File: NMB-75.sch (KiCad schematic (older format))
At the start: 20 parts

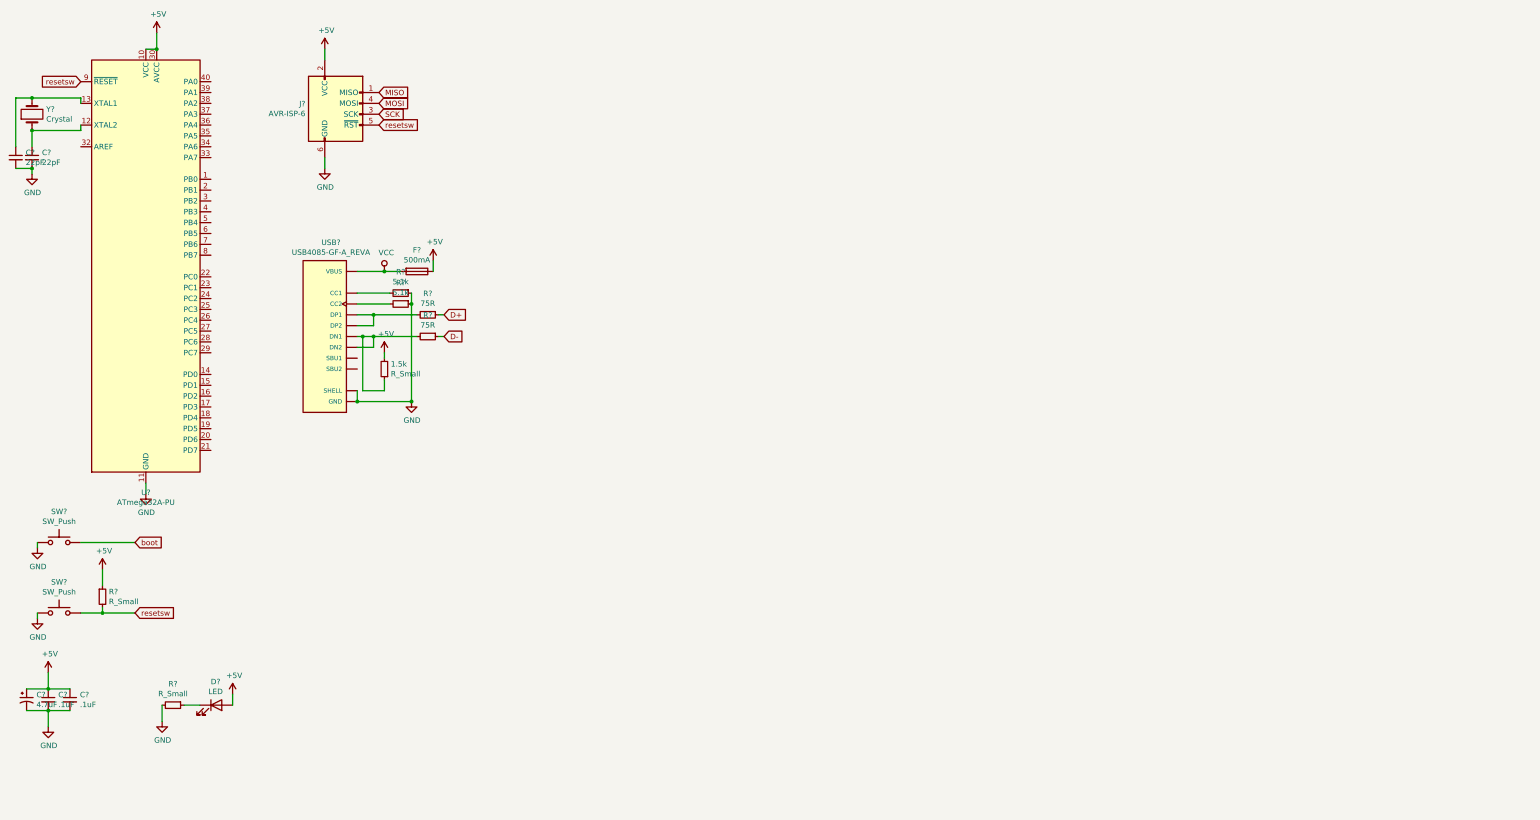
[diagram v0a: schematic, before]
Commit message: schematic work
placed down switches for matrix
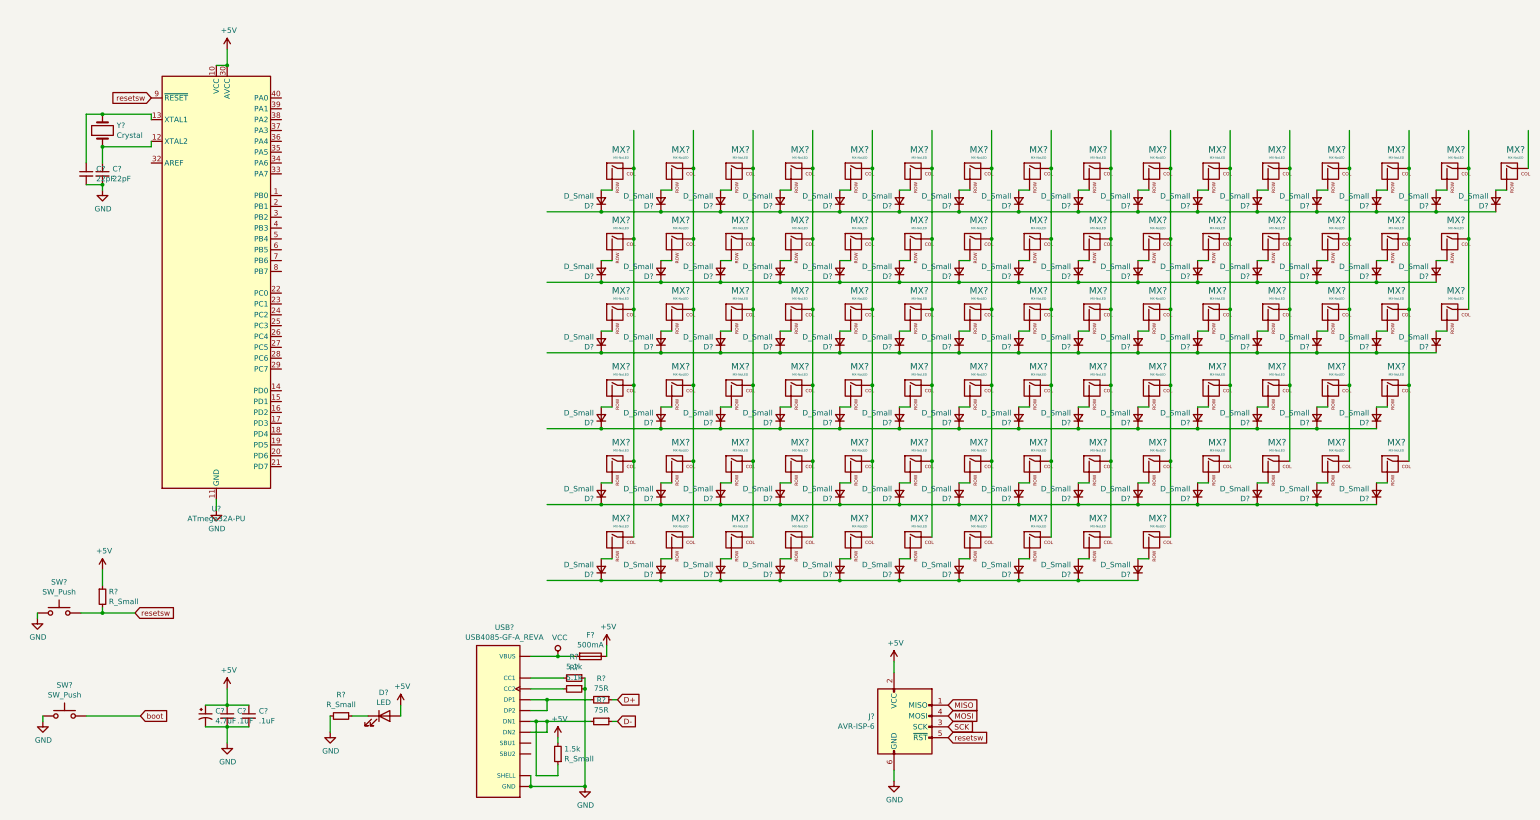
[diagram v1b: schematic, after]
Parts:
- added D? (x84): D_Small, symbol Device:D_Small
- added MX? (x84): MX-NoLED, symbol MX_Alps_Hybrid:MX-NoLED
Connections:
- wire segments 54 -> 306
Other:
- moved on the sheet: 1.5k, C?, D?, F?, J?, R?, SW?, U?, USB?, Y?

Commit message: changed matrix staggering
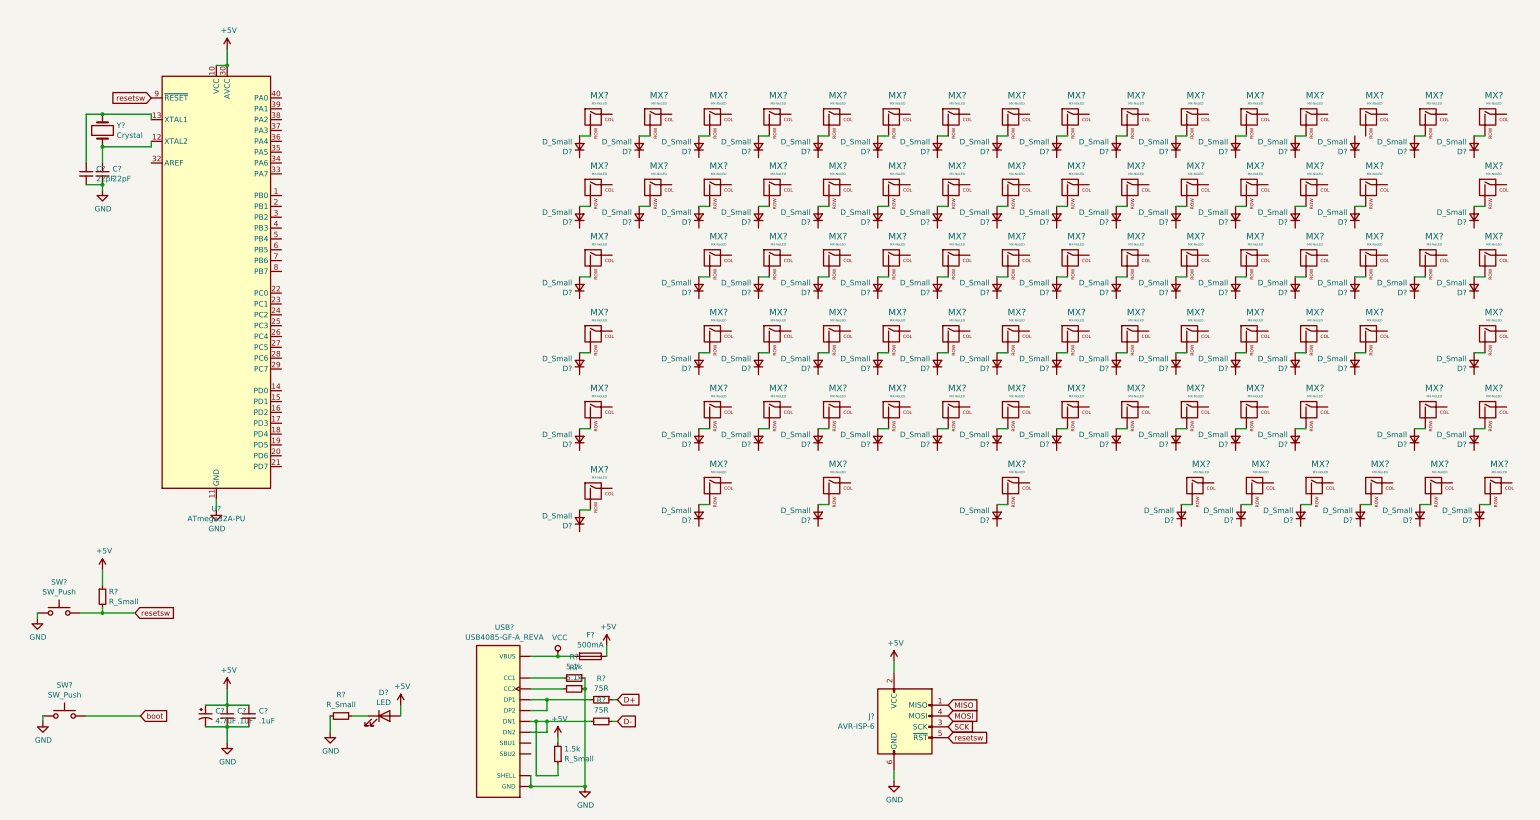
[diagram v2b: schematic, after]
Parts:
- removed D? (x5): D_Small, symbol Device:D_Small
- added D? (x5): D_Small, symbol Device:D_Small
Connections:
- wire segments 306 -> 137
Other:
- moved on the sheet: D?, MX?

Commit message: Footprint assignment progress
added some footprint libraries, assigned some foot prints.
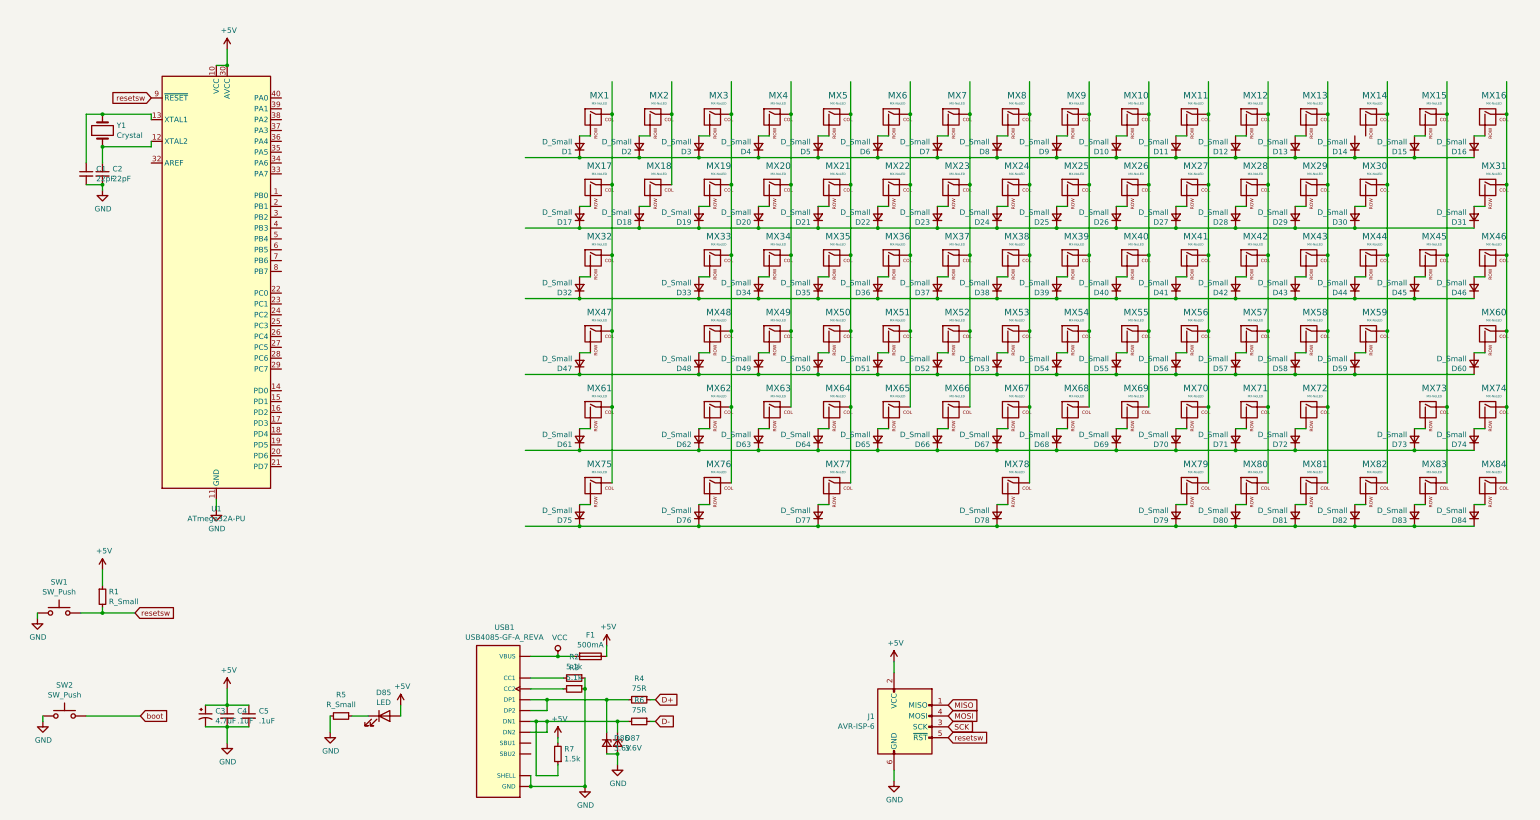
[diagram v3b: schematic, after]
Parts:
- added D86, D87: 3.6V, symbol Device:D_Zener_Small
- D1, D10, D11, D12, D13, D14, D15, D16, D17, D18, D19, D2, D20, D21, D22, D23, D24, D25, D26, D27, D28, D29, D3, D30, D31, D32, D33, D34, D35, D36, D37, D38, D39, D4, D40, D41, D42, D43, D44, D45, D46, D47, D48, D49, D5, D50, D51, D52, D53, D54, D55, D56, D57, D58, D59, D6, D60, D61, D62, D63, D64, D65, D66, D67, D68, D69, D7, D70, D71, D72, D73, D74, D75, D76, D77, D78, D79, D8, D80, D81, D82, D83, D84, D9: renamed from D?; footprint (none) -> Diode_THT:D_DO-35_SOD27_P5.08mm_Vertical_KathodeUp
- F1: renamed from F?; footprint (none) -> libraries:polyfuse_5.1mm
- J1: renamed from J?; footprint (none) -> libraries:AVR_ICSP_3x2
- MX1, MX10, MX11, MX12, MX13, MX14, MX15, MX16, MX17, MX18, MX19, MX2, MX20, MX21, MX22, MX23, MX24, MX25, MX26, MX27, MX28, MX29, MX3, MX31, MX33, MX34, MX35, MX36, MX37, MX38, MX39, MX4, MX40, MX41, MX42, MX43, MX44, MX46, MX48, MX49, MX5, MX50, MX51, MX52, MX53, MX54, MX55, MX56, MX57, MX58, MX6, MX60, MX62, MX63, MX64, MX65, MX66, MX67, MX68, MX69, MX7, MX70, MX71, MX73, MX74, MX79, MX8, MX80, MX81, MX82, MX83, MX84, MX9: renamed from MX?; footprint (none) -> MX_Only:MXOnly-1U-NoLED
- MX30: renamed from MX?; footprint (none) -> MX_Only:MXOnly-2U-NoLED
- MX32, MX45: renamed from MX?; footprint (none) -> MX_Only:MXOnly-1.5U-NoLED
- MX47, MX72: renamed from MX?; footprint (none) -> MX_Only:MXOnly-1.75U-NoLED
- MX59, MX61: renamed from MX?; footprint (none) -> MX_Only:MXOnly-2.25U-NoLED
- MX75, MX76, MX77: renamed from MX?; footprint (none) -> MX_Only:MXOnly-1.25U-NoLED
- MX78: renamed from MX?; footprint (none) -> MX_Only:MXOnly-6.25U-NoLED
- R7: renamed from 1.5k; value R_Small -> 1.5k
- SW1, SW2: renamed from SW?; footprint (none) -> libraries:SW_PUSH_6mm
- USB1: renamed from USB?; footprint GCT_USB4085-GF-A_REVA -> USB4085-GF-A_REVA:GCT_USB4085-GF-A_REVA
- gave numbers to parts that had none: 14
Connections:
- wire segments 137 -> 311
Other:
- moved on the sheet: D75, D79, D80, D81, D82, D83, D84, MX75, MX79, MX80, MX81, MX82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
